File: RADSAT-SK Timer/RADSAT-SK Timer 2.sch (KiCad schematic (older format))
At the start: 35 parts, among them J201 Conn_01x04, J203 Conn_01x02, Q201 IRLML2060, SW205 SW_Push, SW206 SW_Push, U201 LP2980IM5-5.0, U202 LTC3440EMSPBF, U203 TPS3700DDCR

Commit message: Pc bresize (#7)
* PCB has been resized and the layer redone to fit the new shape, assumed a cent                                                                                                                                                                                  red stack for the main connector. No rounded edges.

* figured out how to do rounded corners also pull request test

* Rounded corners X24
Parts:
- removed C201: 1uF, Capacitor_SMD:C_0805_2012Metric, symbol Device:C
- removed C202: 7pF, Capacitor_SMD:C_0805_2012Metric, symbol Device:C
- removed C203: 2.2uF, Capacitor_SMD:C_0805_2012Metric, symbol Device:C
- removed C206: 0.1uF, Capacitor_SMD:C_0805_2012Metric, symbol Device:C
- removed D201: LED, LED_SMD:LED_0805_2012Metric, symbol Device:LED
- removed D202: RB751V40T1G, Diode_SMD:D_SOD-323, symbol Device:D_Schottky
- removed R201: 76.8k, Resistor_SMD:R_0805_2012Metric, symbol Device:R
- removed R202: 51.1k, Resistor_SMD:R_0805_2012Metric, symbol Device:R
- removed R203: 1k, Resistor_SMD:R_0805_2012Metric, symbol Device:R
- removed R204: 560, Resistor_SMD:R_0805_2012Metric, symbol Device:R
- removed R206: 604K, Resistor_SMD:R_0805_2012Metric, symbol Device:R
- removed R207: 49.9k, Resistor_SMD:R_0805_2012Metric, symbol Device:R
- removed R208: 100k, Resistor_SMD:R_0805_2012Metric, symbol Device:R
- removed R210: 10k, Resistor_SMD:R_0805_2012Metric, symbol Device:R
- removed U201: LP2980IM5-5.0, Package_TO_SOT_SMD:TSOT-23-5, symbol LP2980IM5-5.0:LP2980IM5-5.0
- removed U203: TPS3700DDCR, Package_TO_SOT_SMD:TSOT-23-6, symbol TPS3700DDCR:TPS3700DDCR
- added SW201, SW202, SW203, SW205: SW_Push, Connector_Molex:Molex_Micro-Fit_3.0_43650-0200_1x02_P3.00mm_Horizontal, symbol Switch:SW_Push
- D203: symbol Diode:MBR1020VL -> RADSAT-SK-Timer-rescue:MBR1020VL-Diode
- Q201: symbol Transistor_FET:IRLML2060 -> RADSAT-SK-Timer-rescue:IRLML2060-Transistor_FET
- U202: symbol LTC3440EMSPBF:LTC3440EMSPBF -> RADSAT-SK-Timer-rescue:LTC3440EMSPBF-LTC3440EMSPBF
- renumbered SW205 to SW204
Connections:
- net labels removed: CHRG_ON-OFF
- wire segments 112 -> 74
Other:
- note added: "Battery Boost, and Inhibits"
- note removed: "Battery Charging, Boost, and Inhibits"
- moved on the sheet: BT201, BT202, SW204, SW206

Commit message: deleted files for a battery holder that we are not using, -had added it myself-  rearanged some of the layout to get outer edge for ports, changed to df13 hirose ports, added dummy usb connector.
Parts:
- added J204: USB_B_Micro, Connector_USB:USB_Micro-B_Molex-105133-0001, symbol Connector:USB_B_Micro
- J201: footprint Connector_Molex:Molex_Micro-Fit_3.0_43650-0400_1x04_P3.00mm_Horizontal -> Connector_Hirose:Hirose_DF13-04P-1.25DSA_1x04_P1.25mm_Vertical
- J203, SW201, SW202, SW203, SW204, SW205, SW206: footprint Connector_Molex:Molex_Micro-Fit_3.0_43650-0200_1x02_P3.00mm_Horizontal -> Connector_Hirose:Hirose_DF13-02P-1.25DSA_1x02_P1.25mm_Vertical
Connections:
- wire segments 74 -> 76
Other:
- moved on the sheet: BT201, BT202, SW201, SW202, SW203, SW204
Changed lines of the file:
@@
 L Device:Battery_Cell BT202
 U 1 1 600CC811
-P 5150 3700
-F 0 "BT202" H 5268 3796 50  0000 L CNN
-F 1 "Battery_Cell" H 5268 3705 50  0000 L CNN
-F 2 "Battery:BatteryHolder_Keystone_1060_1x2032" V 5150 3760 50  0001 C CNN
-F 3 "~" V 5150 3760 50  0001 C CNN
-	1    5150 3700
+P 5175 3125
+F 0 "BT202" H 5293 3221 50  0000 L CNN
+F 1 "Battery_Cell" H 5293 3130 50  0000 L CNN
+F 2 "Battery:BatteryHolder_Keystone_1060_1x2032" V 5175 3185 50  0001 C CNN
+F 3 "~" V 5175 3185 50  0001 C CNN
+	1    5175 3125
 	1    0    0    -1
 $EndComp
@@
 L Device:Battery_Cell BT201
 U 1 1 600C995D
-P 4425 3700
-F 0 "BT201" H 4543 3796 50  0000 L CNN
-F 1 "Battery_Cell" H 4543 3705 50  0000 L CNN
-F 2 "Battery:BatteryHolder_Keystone_1060_1x2032" V 4425 3760 50  0001 C CNN
-F 3 "~" V 4425 3760 50  0001 C CNN
-	1    4425 3700
+P 4450 3125
+F 0 "BT201" H 4568 3221 50  0000 L CNN
+F 1 "Battery_Cell" H 4568 3130 50  0000 L CNN
+F 2 "Battery:BatteryHolder_Keystone_1060_1x2032" V 4450 3185 50  0001 C CNN
+F 3 "~" V 4450 3185 50  0001 C CNN
+	1    4450 3125
 	1    0    0    -1
 $EndComp
@@
 F 0 "SW206" V 4954 4498 50  0000 L CNN
 F 1 "SW_Push" V 5045 4498 50  0000 L CNN
-F 2 "Connector_Molex:Molex_Micro-Fit_3.0_43650-0200_1x02_P3.00mm_Horizontal" H 5000 4550 50  0001 C CNN
+F 2 "Connector_Hirose:Hirose_DF13-02P-1.25DSA_1x02_P1.25mm_Vertical" H 5000 4550 50  0001 C CNN
 F 3 "~" H 5000 4550 50  0001 C CNN
 	1    5000 4350
@@
 L Switch:SW_Push SW204
 U 1 1 6012B10E
-P 5050 3000
-F 0 "SW204" V 5004 3148 50  0000 L CNN
-F 1 "SW_Push" V 5095 3148 50  0000 L CNN
-F 2 "Connector_Molex:Molex_Micro-Fit_3.0_43650-0200_1x02_P3.00mm_Horizontal" H 5050 3200 50  0001 C CNN
-F 3 "~" H 5050 3200 50  0001 C CNN
-	1    5050 3000
+P 5075 2425
+F 0 "SW204" V 5029 2573 50  0000 L CNN
+F 1 "SW_Push" V 5120 2573 50  0000 L CNN
+F 2 "Connector_Hirose:Hirose_DF13-02P-1.25DSA_1x02_P1.25mm_Vertical" H 5075 2625 50  0001 C CNN
+F 3 "~" H 5075 2625 50  0001 C CNN
+	1    5075 2425
 	0    1    1    0
 $EndComp
@@
 Wire Wire Line
 	6300 2025 6300 1850
-Wire Wire Line
-	6300 1850 7700 1850
 $Comp
 L RADSAT-SK-Timer-rescue:MBR1020VL-Diode D203
@@
 $EndComp
 Wire Wire Line
-	4425 3500 4800 3500
+	4450 2925 4825 2925
 Wire Wire Line
 	4775 4550 4775 4700
-Wire Wire Line
-	4775 3800 4775 4150
-Connection ~ 4800 3500
-Wire Wire Line
-	4800 3500 5150 3500
+Connection ~ 4825 2925
+Wire Wire Line
+	4825 2925 5175 2925
 Text Notes 7400 7500 0    50   ~ 0
 RADSAT-SK Timer Schematic 2
@@
 F 0 "J201" H 1955 7092 50  0000 L CNN
 F 1 "Conn_01x04" H 1955 7001 50  0000 L CNN
-F 2 "Connector_Molex:Molex_Micro-Fit_3.0_43650-0400_1x04_P3.00mm_Horizontal" H 1875 7100 50  0001 C CNN
+F 2 "Connector_Hirose:Hirose_DF13-04P-1.25DSA_1x04_P1.25mm_Vertical" H 1875 7100 50  0001 C CNN
 F 3 "~" H 1875 7100 50  0001 C CNN
 	1    1875 7100
@@
 Antenna Connector
 Wire Notes Line
-	11225 5550 500  5550
+	11125 5000 400  5000
 Text Notes 700  700  0    50   ~ 0
 Battery Boost, and Inhibits
@@
 F 0 "J203" H 4830 7142 50  0000 L CNN
 F 1 "Conn_01x02" H 4830 7051 50  0000 L CNN
-F 2 "Connector_Molex:Molex_Micro-Fit_3.0_43650-0200_1x02_P3.00mm_Horizontal" H 4750 7150 50  0001 C CNN
+F 2 "Connector_Hirose:Hirose_DF13-02P-1.25DSA_1x02_P1.25mm_Vertical" H 4750 7150 50  0001 C CNN
 F 3 "~" H 4750 7150 50  0001 C CNN
 	1    4750 7150
@@
 $EndComp
 Wire Wire Line
-	4800 3200 4800 3500
+	4825 2625 4825 2925
 Wire Wire Line
 	4550 6850 4875 6850
@@
 L Switch:SW_Push SW202
 U 1 1 60B0F6CF
-P 5050 2400
-F 0 "SW202" V 5004 2548 50  0000 L CNN
-F 1 "SW_Push" V 5095 2548 50  0000 L CNN
-F 2 "Connector_Molex:Molex_Micro-Fit_3.0_43650-0200_1x02_P3.00mm_Horizontal" H 5050 2600 50  0001 C CNN
-F 3 "~" H 5050 2600 50  0001 C CNN
-	1    5050 2400
+P 5075 1825
+F 0 "SW202" V 5029 1973 50  0000 L CNN
+F 1 "SW_Push" V 5120 1973 50  0000 L CNN
+F 2 "Connector_Hirose:Hirose_DF13-02P-1.25DSA_1x02_P1.25mm_Vertical" H 5075 2025 50  0001 C CNN
+F 3 "~" H 5075 2025 50  0001 C CNN
+	1    5075 1825
 	0    1    1    0
 $EndComp
@@
 L Switch:SW_Push SW203
 U 1 1 60B0F765
-P 4550 3000
-F 0 "SW203" V 4504 3148 50  0000 L CNN
-F 1 "SW_Push" V 4595 3148 50  0000 L CNN
-F 2 "Connector_Molex:Molex_Micro-Fit_3.0_43650-0200_1x02_P3.00mm_Horizontal" H 4550 3200 50  0001 C CNN
-F 3 "~" H 4550 3200 50  0001 C CNN
-	1    4550 3000
+P 4575 2425
+F 0 "SW203" V 4529 2573 50  0000 L CNN
+F 1 "SW_Push" V 4620 2573 50  0000 L CNN
+F 2 "Connector_Hirose:Hirose_DF13-02P-1.25DSA_1x02_P1.25mm_Vertical" H 4575 2625 50  0001 C CNN
+F 3 "~" H 4575 2625 50  0001 C CNN
+	1    4575 2425
 	0    1    1    0
 $EndComp
@@
 L Switch:SW_Push SW201
 U 1 1 60B0F7F8
-P 4550 2400
-F 0 "SW201" V 4504 2548 50  0000 L CNN
-F 1 "SW_Push" V 4595 2548 50  0000 L CNN
-F 2 "Connector_Molex:Molex_Micro-Fit_3.0_43650-0200_1x02_P3.00mm_Horizontal" H 4550 2600 50  0001 C CNN
-F 3 "~" H 4550 2600 50  0001 C CNN
-	1    4550 2400
+P 4575 1825
+F 0 "SW201" V 4529 1973 50  0000 L CNN
+F 1 "SW_Push" V 4620 1973 50  0000 L CNN
+F 2 "Connector_Hirose:Hirose_DF13-02P-1.25DSA_1x02_P1.25mm_Vertical" H 4575 2025 50  0001 C CNN
+F 3 "~" H 4575 2025 50  0001 C CNN
+	1    4575 1825
 	0    1    1    0
 $EndComp
@@
 F 0 "SW205" V 4454 4498 50  0000 L CNN
 F 1 "SW_Push" V 4545 4498 50  0000 L CNN
-F 2 "Connector_Molex:Molex_Micro-Fit_3.0_43650-0200_1x02_P3.00mm_Horizontal" H 4500 4550 50  0001 C CNN
+F 2 "Connector_Hirose:Hirose_DF13-02P-1.25DSA_1x02_P1.25mm_Vertical" H 4500 4550 50  0001 C CNN
 F 3 "~" H 4500 4550 50  0001 C CNN
 	1    4500 4350
@@
 $EndComp
 Wire Wire Line
-	5050 2800 4800 2800
-Wire Wire Line
-	4550 2600 4800 2600
-Wire Wire Line
-	4550 2200 4800 2200
-Wire Wire Line
-	4550 3200 4800 3200
-Wire Wire Line
-	4800 2600 4800 2800
-Connection ~ 4800 2600
-Wire Wire Line
-	4800 2600 5050 2600
-Connection ~ 4800 2800
-Wire Wire Line
-	4800 2800 4550 2800
-Wire Wire Line
-	4500 4150 4775 4150
+	5075 2225 4825 2225
+Wire Wire Line
+	4575 2025 4825 2025
+Wire Wire Line
+	4575 1625 4825 1625
+Wire Wire Line
+	4575 2625 4825 2625
+Wire Wire Line
+	4825 2025 4825 2225
+Connection ~ 4825 2025
+Wire Wire Line
+	4825 2025 5075 2025
+Connection ~ 4825 2225
+Wire Wire Line
+	4825 2225 4575 2225
 Wire Wire Line
 	4500 4550 4775 4550
@@
 	4775 4550 5000 4550
 Wire Wire Line
-	4425 3800 4775 3800
-Connection ~ 4775 3800
-Wire Wire Line
-	4775 3800 5150 3800
-Connection ~ 4775 4150
-Wire Wire Line
-	4775 4150 5000 4150
-Connection ~ 4800 3200
-Wire Wire Line
-	4800 3200 5050 3200
-Wire Wire Line
-	4800 2200 4800 2025
-Wire Wire Line
-	4800 2025 6300 2025
-Connection ~ 4800 2200
-Wire Wire Line
-	4800 2200 5050 2200
+	4450 3225 4800 3225
+Connection ~ 4800 3225
+Wire Wire Line
+	4800 3225 5175 3225
+Connection ~ 4825 2625
+Wire Wire Line
+	4825 2625 5075 2625
+Wire Wire Line
+	4825 1625 4825 1450
+Wire Wire Line
+	4825 1450 6325 1450
+Connection ~ 4825 1625
+Wire Wire Line
+	4825 1625 5075 1625
+Wire Wire Line
+	4500 4150 4800 4150
+Wire Wire Line
+	6325 1450 6325 1850
+Wire Wire Line
+	6300 1850 6325 1850
+Connection ~ 6325 1850
+Wire Wire Line
+	6325 1850 7700 1850
+Wire Wire Line
+	4800 3225 4800 4150
+Connection ~ 4800 4150
+Wire Wire Line
+	4800 4150 5000 4150
+$Comp
+L Connector:USB_B_Micro J204
+U 1 1 60C6CBAB
+P 925 5600
+F 0 "J204" H 980 6067 50  0000 C CNN
+F 1 "USB_B_Micro" H 980 5976 50  0000 C CNN
+F 2 "Connector_USB:USB_Micro-B_Molex-105133-0001" H 1075 5550 50  0001 C CNN
+F 3 "~" H 1075 5550 50  0001 C CNN
+	1    925  5600
+	1    0    0    -1
+$EndComp
 $EndSCHEMATC

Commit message: Deleted a bunch of backups and unnecessary project files
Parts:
- D203: symbol RADSAT-SK-Timer-rescue:MBR1020VL-Diode -> RADSAT-SK-Timer-rescue:MBR1020VL-Diode-RADSAT-SK-Timer-rescue
- J204: symbol Connector:USB_B_Micro -> RADSAT-SK-Timer-rescue:USB_B_Micro-Connector-RADSAT-SK-Timer-rescue
- Q201: symbol RADSAT-SK-Timer-rescue:IRLML2060-Transistor_FET -> RADSAT-SK-Timer-rescue:IRLML2060-Transistor_FET-RADSAT-SK-Timer-rescue
- U202: symbol RADSAT-SK-Timer-rescue:LTC3440EMSPBF-LTC3440EMSPBF -> RADSAT-SK-Timer-rescue:LTC3440EMSPBF-LTC3440EMSPBF-RADSAT-SK-Timer-rescue
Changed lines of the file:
@@
 EESchema Schematic File Version 4
-LIBS:RADSAT-SK Timer-cache
-EELAYER 26 0
+EELAYER 30 0
 EELAYER END
 $Descr A4 11693 8268
@@
 $EndComp
 $Comp
-L RADSAT-SK-Timer-rescue:LTC3440EMSPBF-LTC3440EMSPBF U202
+L RADSAT-SK-Timer-rescue:LTC3440EMSPBF-LTC3440EMSPBF-RADSAT-SK-Timer-rescue U202
 U 1 1 6019F249
 P 8400 2100
+AR Path="/6019F249" Ref="U202"  Part="1"
+AR Path="/602E25D3/6019F249" Ref="U202"  Part="1"
 F 0 "U202" H 8400 2375 50  0000 C CNN
 F 1 "LTC3440EMSPBF" H 8400 2275 50  0000 C CNN
@@
 $EndComp
 $Comp
-L RADSAT-SK-Timer-rescue:IRLML2060-Transistor_FET Q201
+L RADSAT-SK-Timer-rescue:IRLML2060-Transistor_FET-RADSAT-SK-Timer-rescue Q201
 U 1 1 600FFF1C
 P 7000 2500
+AR Path="/600FFF1C" Ref="Q201"  Part="1"
+AR Path="/602E25D3/600FFF1C" Ref="Q201"  Part="1"
 F 0 "Q201" H 6925 2300 50  0000 L CNN
 F 1 "IRLML2060" H 6650 2375 50  0000 L CNN
@@
 	6300 2025 6300 1850
 $Comp
-L RADSAT-SK-Timer-rescue:MBR1020VL-Diode D203
+L RADSAT-SK-Timer-rescue:MBR1020VL-Diode-RADSAT-SK-Timer-rescue D203
 U 1 1 60121A1E
 P 9400 1425
+AR Path="/60121A1E" Ref="D203"  Part="1"
+AR Path="/602E25D3/60121A1E" Ref="D203"  Part="1"
 F 0 "D203" H 9400 1209 50  0000 C CNN
 F 1 "MBRM1020T3" H 9400 1300 50  0000 C CNN
@@
 	4800 4150 5000 4150
 $Comp
-L Connector:USB_B_Micro J204
+L RADSAT-SK-Timer-rescue:USB_B_Micro-Connector-RADSAT-SK-Timer-rescue J204
 U 1 1 60C6CBAB
 P 925 5600
+AR Path="/60C6CBAB" Ref="J204"  Part="1"
+AR Path="/602E25D3/60C6CBAB" Ref="J204"  Part="1"
 F 0 "J204" H 980 6067 50  0000 C CNN
 F 1 "USB_B_Micro" H 980 5976 50  0000 C CNN

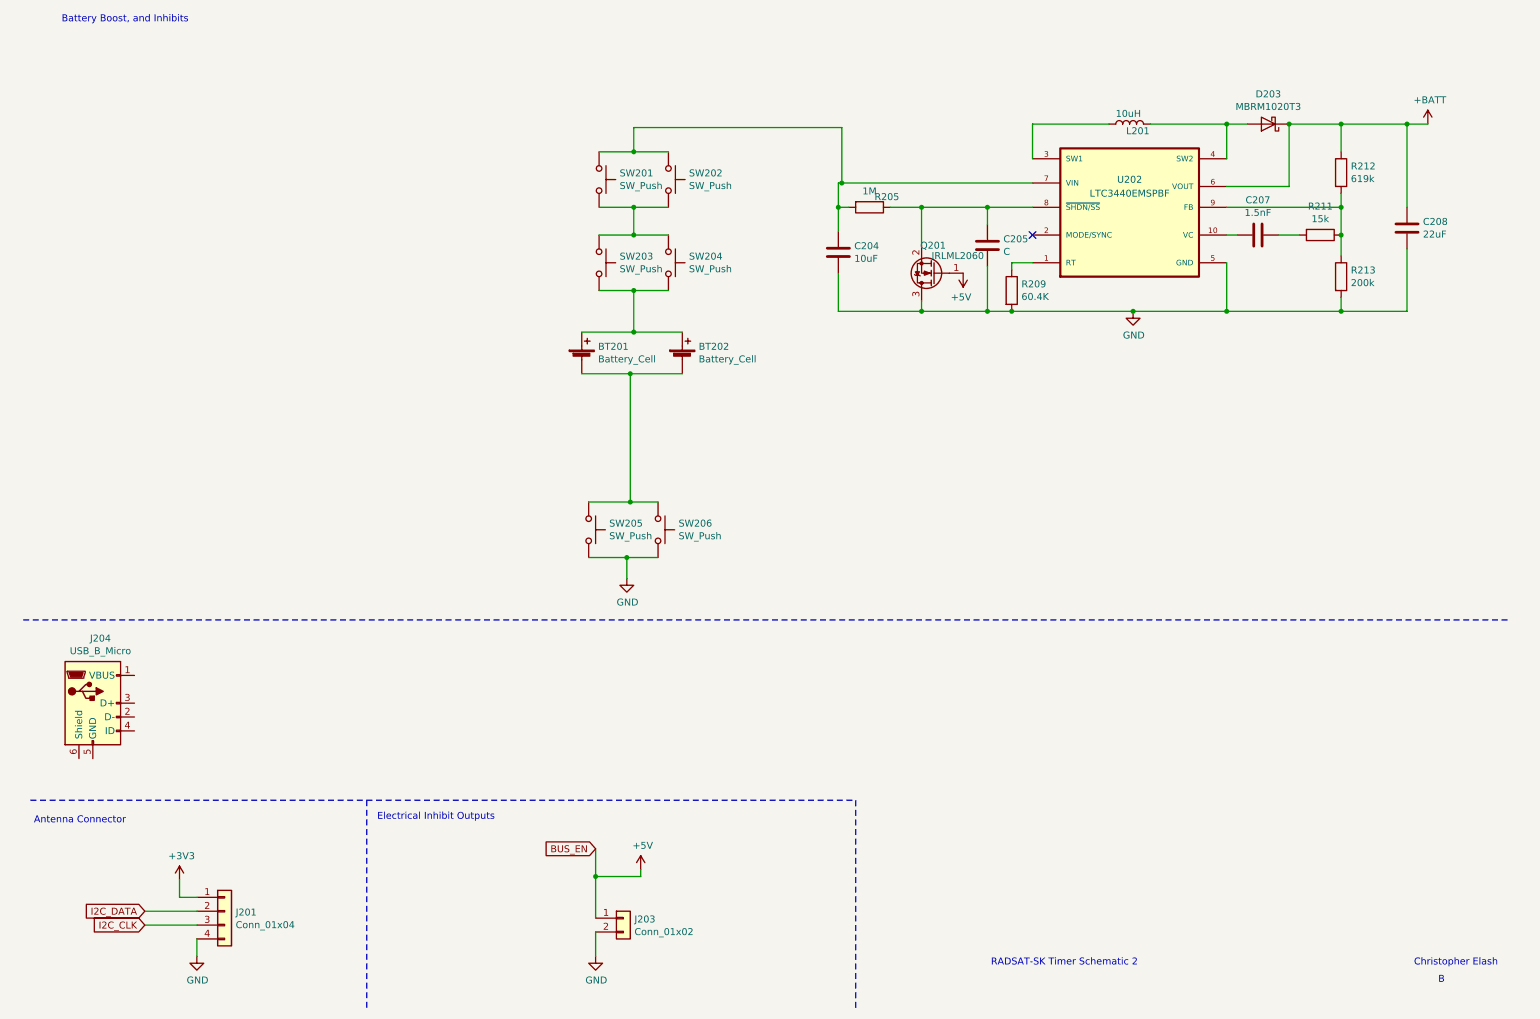
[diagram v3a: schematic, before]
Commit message: Added in the RBF connector and setup to coincells, need to add inhibitor logic and find components
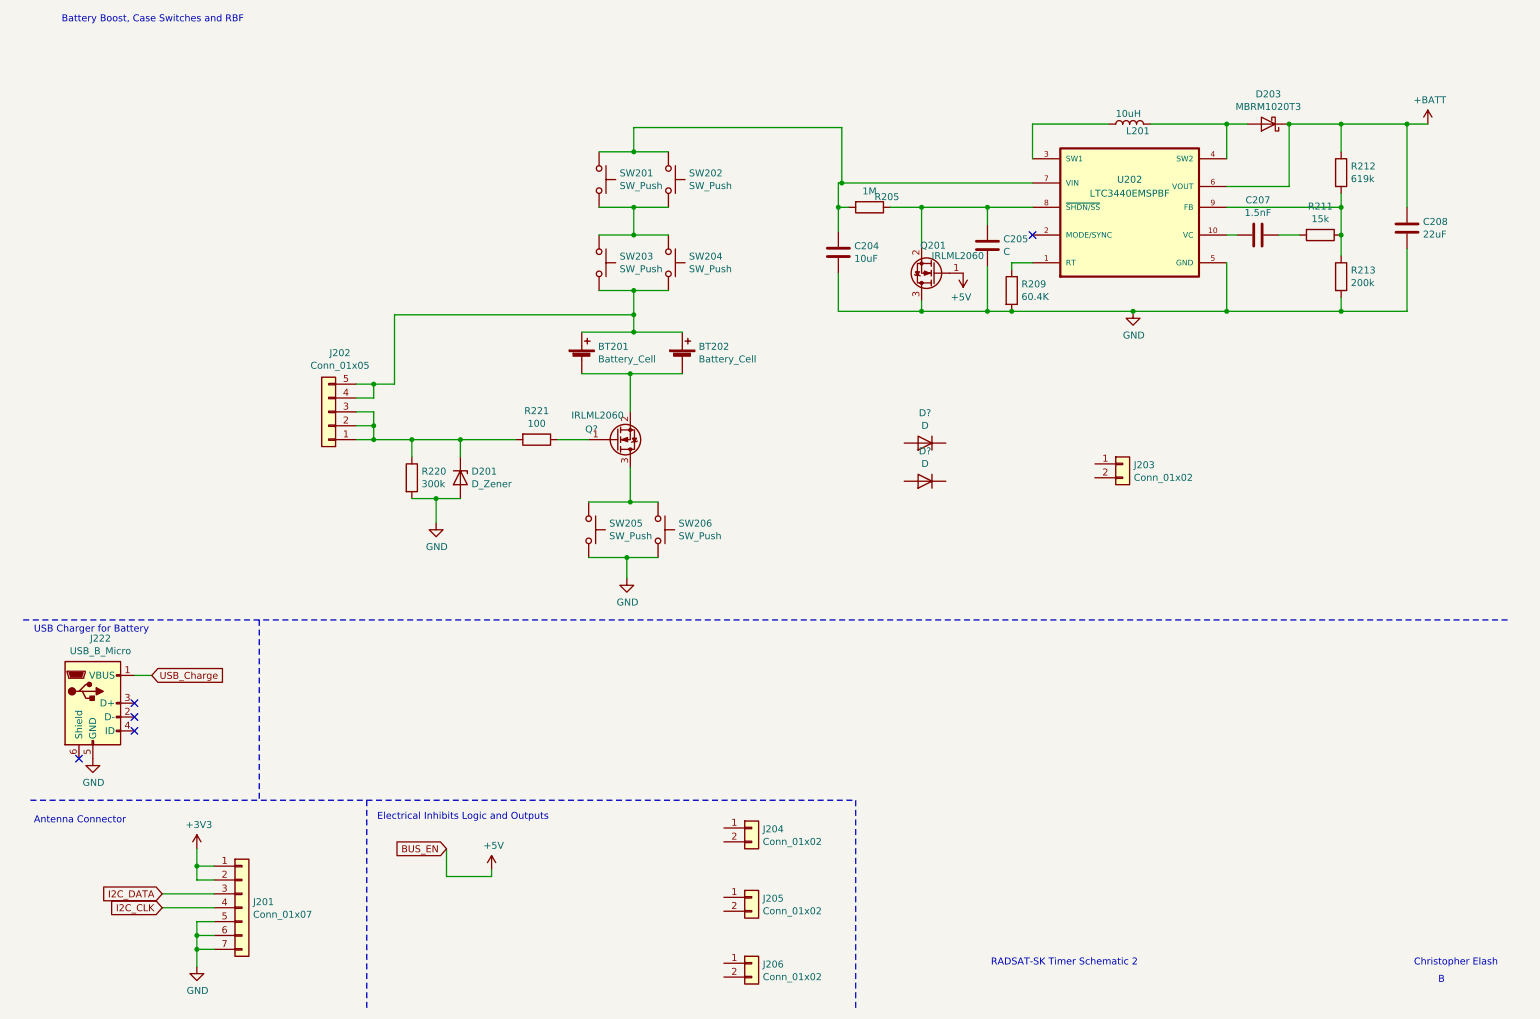
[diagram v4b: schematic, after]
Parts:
- removed J201: Conn_01x04, Connector_Hirose:Hirose_DF13-04P-1.25DSA_1x04_P1.25mm_Vertical, symbol Connector_Generic:Conn_01x04
- added D201: D_Zener, symbol Device:D_Zener
- added D? (x2): D, Diode_SMD:D_0805_2012Metric, symbol Device:D
- added J201: Conn_01x07, symbol Connector_Generic:Conn_01x07
- added J202: Conn_01x05, symbol Connector_Generic:Conn_01x05
- added J203, J205, J206: Conn_01x02, Connector_Hirose:Hirose_DF13-02P-1.25DSA_1x02_P1.25mm_Vertical, symbol Connector_Generic:Conn_01x02
- added Q?: IRLML2060, Package_TO_SOT_SMD:SOT-23, symbol Transistor_FET:IRLML2060
- added R220: 300k, symbol Device:R
- added R221: 100, symbol Device:R
- renumbered J203 to J204
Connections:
- net +3V3: now also J201.1 (Pin_1), J201.2 (Pin_2)
- net +5V: no longer J204.1 (Pin_1)
- net GND: now also J204.5 (GND), D201.2 (A), J201.5 (Pin_5), J201.6 (Pin_6), J201.7 (Pin_7), R220.2; no longer J204.2 (Pin_2)
- net I2C_CLK: now also J201.4 (Pin_4)
- net I2C_DATA: now also J201.3 (Pin_3)
- net at BT201.1 (+), BT202.1 (+), SW203.2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: now also J202.4 (Pin_4), J202.5 (Pin_5)
- net at BT201.2 (-), BT202.2 (-): now also Q?.2 (S); no longer SW205.1, SW206.1
- net USB_Charge: now reaches J204.1 (VBUS)
- new net: Q?.3 (D), SW205.1, SW206.1
- new net: D201.1 (K), J202.1 (Pin_1), J202.2 (Pin_2), J202.3 (Pin_3), R220.1, R221.2
- new net: Q?.1 (G), R221.1
- no-connect marks 1 -> 5
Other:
- note added: "Battery Boost, Case Switches and RBF"
- note added: "Electrical Inhibits Logic and Outputs"
- note added: "USB Charger for Battery"
- note removed: "Battery Boost, and Inhibits"
- note removed: "Electrical Inhibit Outputs"
- moved on the sheet: J204
